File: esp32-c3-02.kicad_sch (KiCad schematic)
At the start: 25 parts, among them J3 GSD090012SEU, U3 ESP32-C3-WROOM-02-H4, U4 CP2102N-Axx-xQFN20, U5 USBLC6-2SC6, U6 W25Q32JVSSIQ

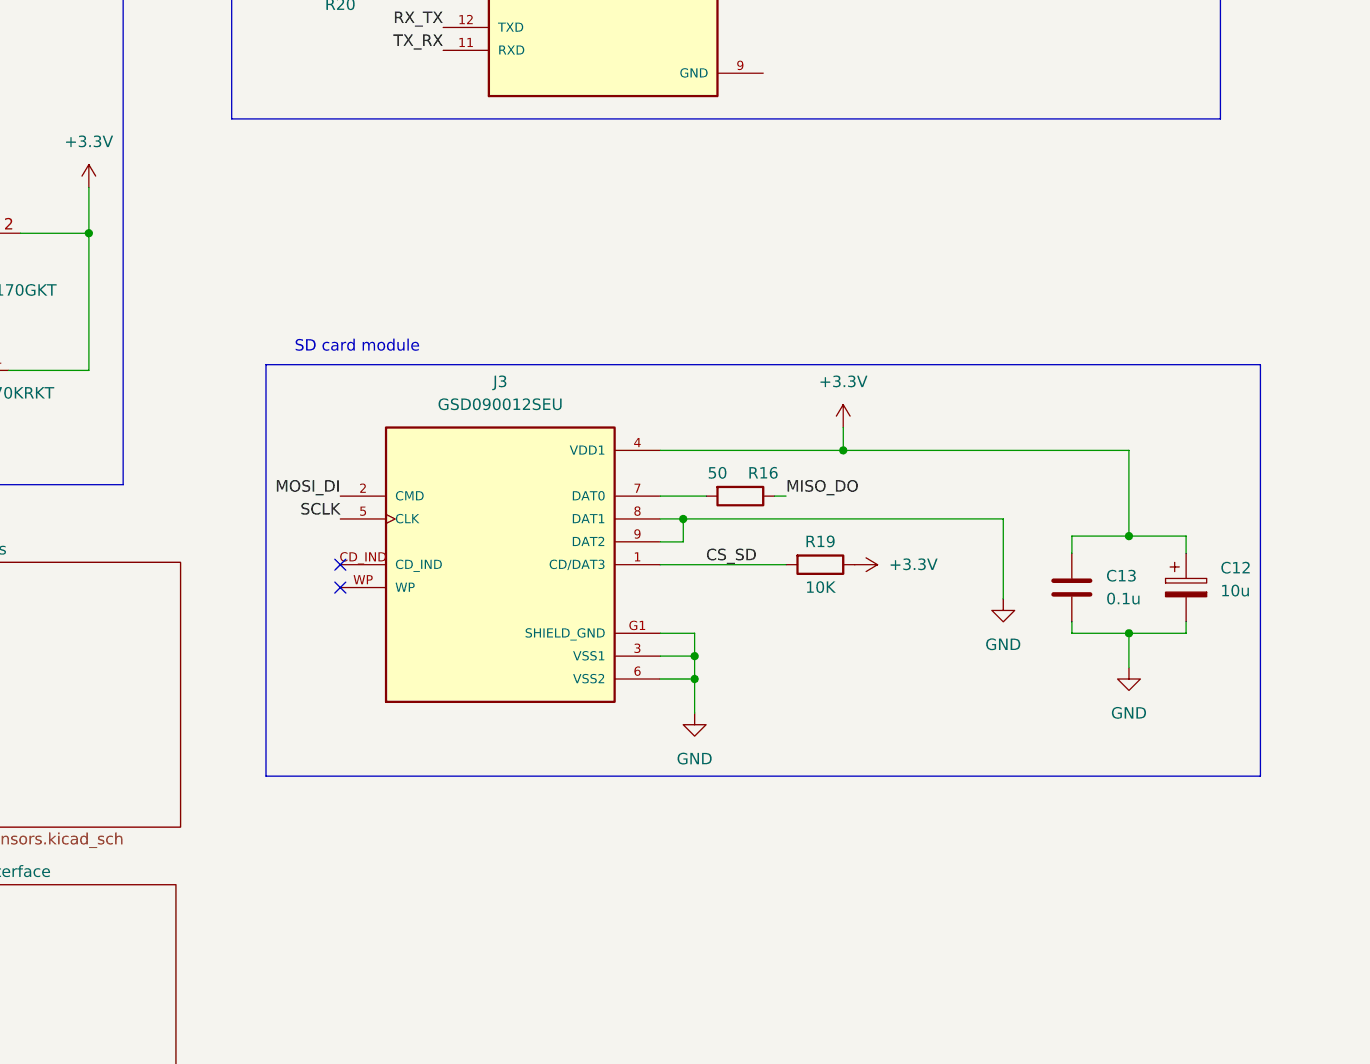
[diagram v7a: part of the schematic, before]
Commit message: 1.2.6 Add test points
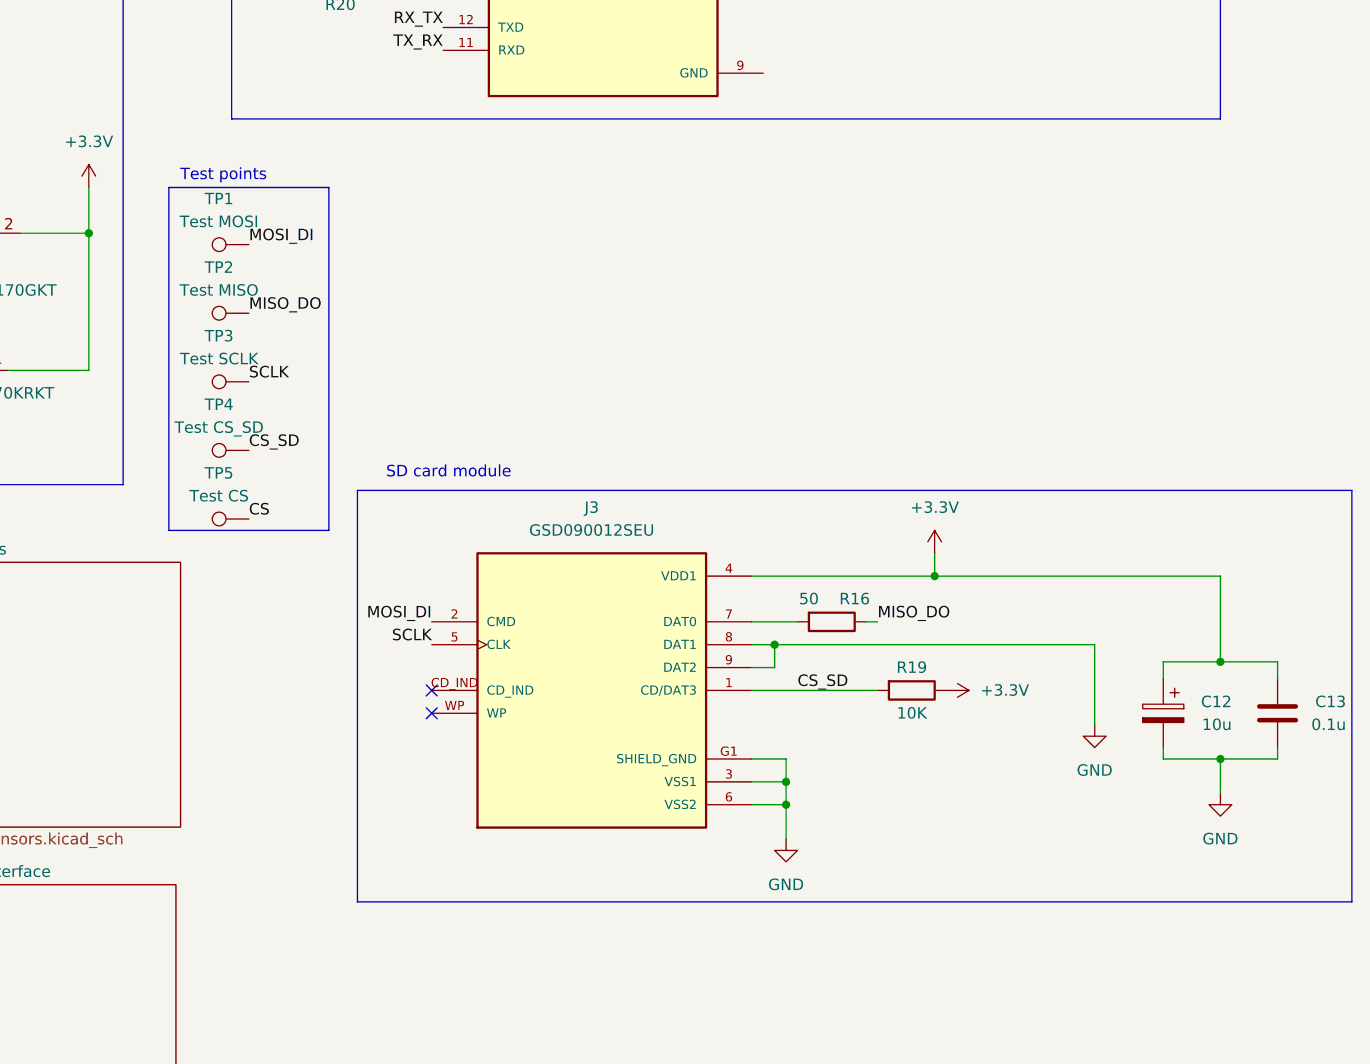
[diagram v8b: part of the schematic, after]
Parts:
- added TP1: Test MOSI, symbol Connector:TestPoint
- added TP2: Test MISO, symbol Connector:TestPoint
- added TP3: Test SCLK, symbol Connector:TestPoint
- added TP4: Test CS_SD, symbol Connector:TestPoint
- added TP5: Test CS, symbol Connector:TestPoint
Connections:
- net CS: now also TP5.1
- net CS_SD: now also TP4.1
- net MISO_DO: now also TP2.1
- net MOSI_DI: now also TP1.1
- net SCLK: now also TP3.1
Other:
- note added: "Test points"
- moved on the sheet: C12, C13, J3, R16, R19
